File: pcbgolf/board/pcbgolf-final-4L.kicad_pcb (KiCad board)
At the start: 2 copper layers, 48.2 x 51 mm, 245 parts, among them J1 DCBARRELSMT, J2 MICRO_SD-0472192001, J3 USB-C-FEMALE, J4 CAN, J5 USB-C-FEMALEGCT, J6 USB-C-FEMALEGCT, J7 USB-C-FEMALEGCT, J8 USB-C-FEMALEGCT, Q1 SIS427-VI, Q2 NFET-DUAL-COMMON-SOURCE-QS5K2, Q3 NFET-DUAL-COMMON-SOURCE-QS5K2, Q4 NFET-DUAL-COMMON-SOURCE-QS5K2, Q5 NFET-DUAL-COMMON-SOURCE-QS5K2, Q6 NFET-DUAL-COMMON-SOURCE-QS5K2, Q7 NFET-DUAL-COMMON-SOURCE-QS5K2, Q8 NFET-DUAL-COMMON-SOURCE-QS5K2, Q9 NFET-DUAL-COMMON-SOURCE-QS5K2, SW1 SPST-2-4PIN, U1 AP62300T, U10 NCS20071XV, U11 NCS20071XV, U12 NCS20071XV, U13 TPS25942, U14 TPS25942, U15 TPS25942, U16 TPS25942, U2 AP62300T, U3 STM32H725ZGTx, U4 USB2517, U5 MCP2542FDT-E/MNY, U6 MCP2542FDT-E/MNY, U7 MCP2542FDT-E/MNY, U8 MCP2542FDT-E/MNY, U9 NCS20071XV, Y1 25MHz, Y2 24MHz

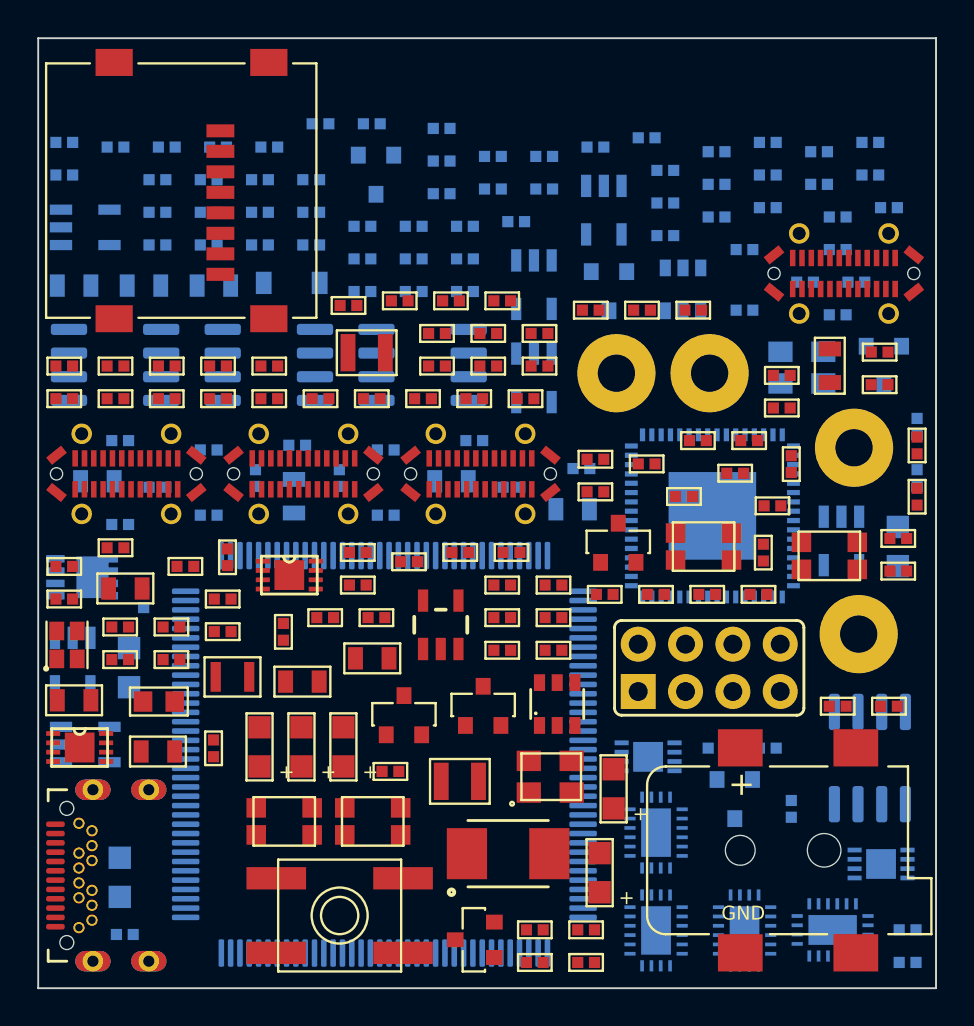
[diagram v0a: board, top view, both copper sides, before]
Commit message: Sync pcbgolf: measured part heights, 3D assembly bounding box, final board
Mirrors lblommesteyn/pcbgolf. The substantive change is that part heights are
now measured from the footprints' own STEP models rather than estimated: the
barrel jack is 11.00 mm, not the 9.00 mm assumed, so Z is 14.35 mm and every
previously reported volume was understated by about 5,300 mm^3.

Also adds bbox3d.py (the real PCBA bounding box, which is what the challenge
scores), step_assembly.py (a STEP built from that same geometry), and the
final LQFP-100 board with R11 not fitted, since the LQFP-100 package has no
PDR_ON pin for it to strap.

Co-Authored-By: Claude Opus 5 <noreply@anthropic.com>
Claude-Session: https://claude.ai/code/session_013nBHDXVrXKghy52w5PgN3h
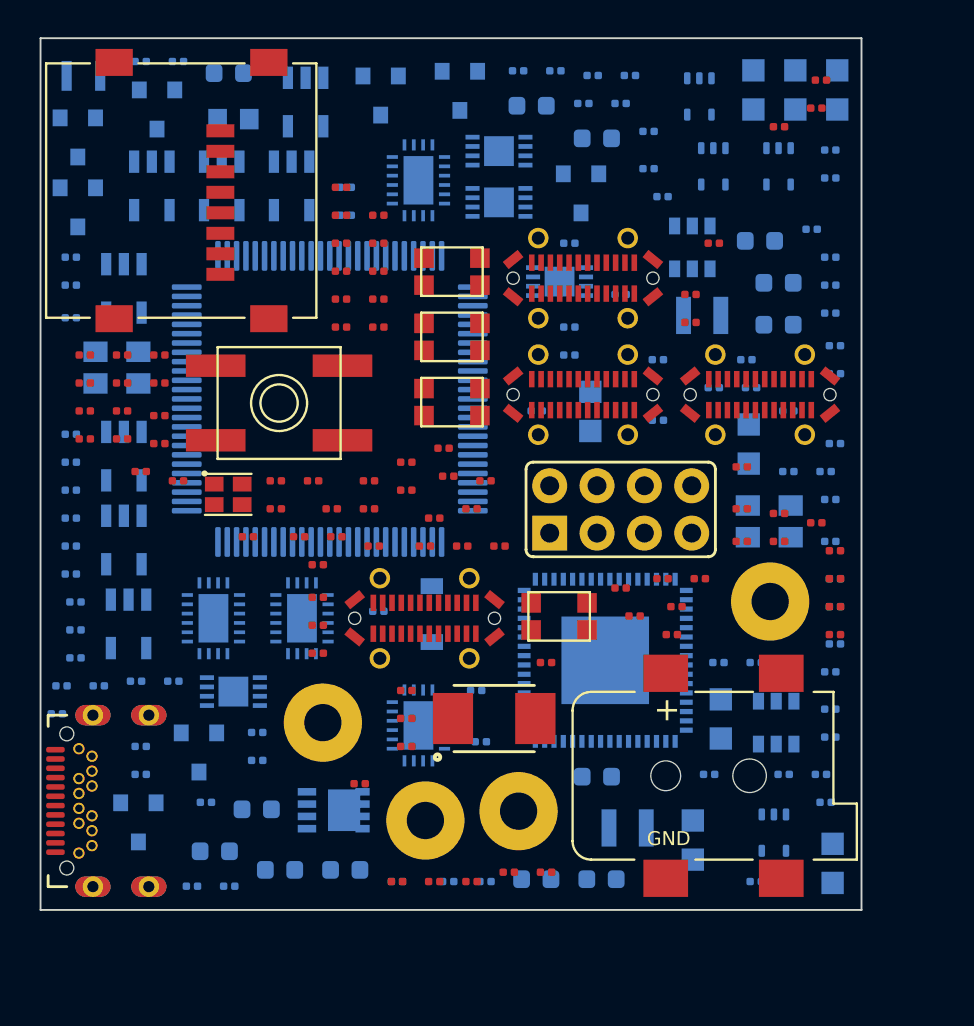
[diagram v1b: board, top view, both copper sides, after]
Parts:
- removed R11: 10k, pcbgolf:0402-R
- C1, C12, C13, C15, C20, C3, C52: footprint pcbgolf:0805-C -> pcbgolf-gen:0603-C
- C10, C14, C16, C17, C22, C23, C26, C27, C28, C29, C32, C35, C36, C38, C4, C43, C44, C45, C46, C47, C48, C49, C6, C9: footprint pcbgolf:0402-C -> pcbgolf-gen:0201-C; moved to F.Cu
- C11, C18, C24, C31, C39: footprint pcbgolf:0402-C -> pcbgolf-gen:0201-C
- C19, C21, C50, C51, C53, C8: footprint pcbgolf:0805-C -> pcbgolf-gen:0603-C; moved to B.Cu
- C2, C25, C30, C33, C34, C37, C40, C41, C42, C5, C7: footprint pcbgolf:0402-C -> pcbgolf-gen:0201-C; moved to B.Cu
- L1, L2, L3, L4, LED10, LED12, LED13, LED14, LED2, LED3, LED4, LED5, LED7, Q6, U1, U5, U7, Y1: moved to B.Cu
- R1, R100, R101, R105, R106, R108, R110, R111, R112, R114, R115, R116, R117, R121, R124, R13, R14, R15, R16, R18, R19, R20, R21, R22, R24, R28, R32, R33, R36, R37, R38, R40, R44, R47, R48, R49, R50, R51, R53, R55, R56, R57, R58, R59, R6, R60, R61, R64, R67, R72, R73, R74, R77, R81, R82, R83, R84, R86, R89, R9, R91, R92, R93, R95, R96, R98: footprint pcbgolf:0402-R -> pcbgolf-gen:0201-R; moved to B.Cu
- R10, R102, R103, R104, R107, R109, R113, R118, R12, R120, R122, R123, R125, R17, R23, R25, R26, R27, R29, R3, R30, R31, R34, R35, R39, R4, R41, R42, R43, R45, R46, R5, R52, R54, R62, R63, R68, R69, R7, R71, R75, R76, R78, R79, R8, R80, R85, R88, R90, R94, R97, R99: footprint pcbgolf:0402-R -> pcbgolf-gen:0201-R; moved to F.Cu
- R119, R2, R65, R66, R70, R87: footprint pcbgolf:0402-R -> pcbgolf-gen:0201-R
- U10, U11, U12, U9: footprint pcbgolf:SOIC-8_3.9x4.9mm_P1.27mm -> pcbgolf-gen:SC70-5
- U3: footprint pcbgolf:LQFP-144_20x20mm_P0.5mm -> pcbgolf-gen:LQFP-100_14x14
- moved R101 49.0 mm to (55.3, 50.9)
- moved LED15 48.3 mm to (56.2, 53.5)
- moved LED13 48.1 mm to (52.0, 55.0), turned to 0 degrees
- moved C10 45.2 mm to (69.1, 94.9)
- moved R31 44.3 mm to (92.6, 77.2)
- moved LED3 44.1 mm to (88.2, 52.5)
- moved LED11 44.1 mm to (52.0, 58.7)
- moved LED2 43.9 mm to (92.7, 52.5)
- moved U14 43.9 mm to (70.2, 57.3)
- moved C16 43.2 mm to (54.3, 71.2)
- moved R71 43.0 mm to (68.1, 65.2)
- moved R24 42.4 mm to (92.3, 87.2)
- moved R36 41.4 mm to (51.1, 84.4)
- moved C27 41.1 mm to (75.1, 94.4)
- moved Q7 40.8 mm to (54.4, 63.1)
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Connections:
- U3 pad 10: (no net) -> VLXSMPS
- U3 pad 100: STM_D_N -> +3V3
- U3 pad 11: (no net) -> +3V3
- U3 pad 12: GND -> VDDLDO
- U3 pad 13: +3V3 -> N$17
- U3 pad 14: GND -> N$33
- U3 pad 15: VLXSMPS -> (no net)
- U3 pad 16: +3V3 -> N$35
- U3 pad 17: VDDLDO -> N$36
- U3 pad 18: GND -> N$37
- U3 pad 19: +3V3 -> N$38
- U3 pad 2: LED_G -> LED_R
- U3 pad 20: (no net) -> +3V3
- U3 pad 21: N$29 -> GND
- U3 pad 22: N$30 -> GND
- U3 pad 23: N$31 -> VDDA
- U3 pad 24: N$32 -> VDDA
- U3 pad 25: N$17 -> CH1_PWR_EN
- U3 pad 26: N$33 -> CH2_PWR_EN
- U3 pad 27: (no net) -> CH2_SBU1_RELAY
- U3 pad 28: N$35 -> CAN2_EN
- U3 pad 29: N$36 -> GND
- U3 pad 3: LED_R -> (no net)
- U3 pad 30: N$37 -> +3V3
- U3 pad 31: N$38 -> CH3_PWR_EN
- U3 pad 32: +3V3 -> CH4_PWR_EN
- U3 pad 33: GND -> CH4_IMON
- U3 pad 34: GND -> CH4_SBU2_IGN
- U3 pad 35: VDDA -> CH1_IMON
- U3 pad 36: VDDA -> N$31
- U3 pad 37: CH1_PWR_EN -> CH3_IMON
- U3 pad 38: CH2_PWR_EN -> CH2_IMON
- U3 pad 4: (no net) -> +3V3
- U3 pad 41: GND -> (no net)
- U3 pad 42: +3V3 -> HUB_SCL
- U3 pad 43: CH3_PWR_EN -> HUB_SDA
- U3 pad 44: CH4_PWR_EN -> VDDLDO
- U3 pad 45: CH4_IMON -> GND
- U3 pad 46: (no net) -> VDDLDO
- U3 pad 47: CH1_IMON -> +3V3
- U3 pad 48: (no net) -> CAN3_RX
- U3 pad 49: (no net) -> CAN3_TX
- U3 pad 5: (no net) -> +3V3
- U3 pad 50: CH2_IMON -> N$29
- U3 pad 51: (no net) -> N$30
- U3 pad 52: CH3_IMON -> CH2_SBU2_IGN
- U3 pad 53: (no net) -> CH3_SBU2_IGN
- U3 pad 54: (no net) -> CH2_SBU2_RELAY
- U3 pad 55: GND -> CH3_SBU1_RELAY
- U3 pad 56: +3V3 -> CAN2_RX
- U3 pad 57: (no net) -> CAN2_TX
- U3 pad 58: (no net) -> GND
- U3 pad 59: (no net) -> +3V3
- U3 pad 6: GND -> (no net)
- U3 pad 60: (no net) -> CH4_SBU1_IGN
- U3 pad 61: (no net) -> CH4_SBU1_RELAY
- U3 pad 62: (no net) -> CH3_SBU1_IGN
- U3 pad 63: (no net) -> CH3_SBU2_RELAY
- U3 pad 64: (no net) -> SD_D0
- U3 pad 65: BTN -> SD_D1
- U3 pad 66: HUB_SCL -> CH4_SBU2_RELAY
- U3 pad 67: HUB_SDA -> BTN
- U3 pad 68: VDDLDO -> LED_G
- U3 pad 69: GND -> STM_D_N
- U3 pad 7: +3V3 -> (no net)
- U3 pad 70: VDDLDO -> STM_D_P
- U3 pad 71: +3V3 -> (no net)
- U3 pad 72: CAN3_RX -> VDDLDO
- U3 pad 73: CAN3_TX -> GND
- U3 pad 74: (no net) -> VDDLDO
- U3 pad 75: (no net) -> +3V3
- U3 pad 76: CH2_SBU2_IGN -> +3V3
- U3 pad 77: CH3_SBU2_IGN -> (no net)
- U3 pad 78: CH2_SBU2_RELAY -> N$32
- U3 pad 79: +3V3 -> SD_D2
- U3 pad 8: +3V3 -> (no net)
- U3 pad 80: GND -> SD_D3
- U3 pad 81: CH3_SBU1_RELAY -> SD_CLK
- U3 pad 82: CH3_SBU1_IGN -> CH1_SBU1_IGN
- U3 pad 83: CH3_SBU2_RELAY -> CH1_SBU1_RELAY
- U3 pad 84: CH4_SBU1_IGN -> SD_CMD
- U3 pad 85: CH4_SBU1_RELAY -> CH1_SBU2_IGN
- U3 pad 86: (no net) -> CH1_SBU2_RELAY
- U3 pad 87: (no net) -> CH2_SBU1_IGN
- U3 pad 88: (no net) -> +3V3
- U3 pad 89: GND -> CAN1_EN
- U3 pad 9: (no net) -> GND
- U3 pad 90: +3V3 -> CAN3_EN
- U3 pad 91: +3V3 -> CAN1_RX
- U3 pad 92: +3V3 -> CAN1_TX
- U3 pad 93: (no net) -> CAN0_EN
- U3 pad 94: (no net) -> BTN
- U3 pad 95: SD_D0 -> CAN0_RX
- U3 pad 96: SD_D1 -> CAN0_TX
- U3 pad 97: (no net) -> VDDLDO
- U3 pad 98: (no net) -> GND
- U3 pad 99: (no net) -> VDDLDO
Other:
- board size 48.2 x 51 mm -> 44 x 46.8 mm
- copper layers 2 -> 4
